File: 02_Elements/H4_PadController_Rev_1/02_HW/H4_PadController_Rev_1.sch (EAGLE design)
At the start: 42 parts

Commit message: Finished H4_PadController_Rev_1 Schematic
The Schematic has been finished! Yay!
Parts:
- added C_MUX: 10uF, adafruit:C-USC1206
- added J_PAD: 22-27-2101-10, con-molex:22-27-2101-10
- added J_PRG: 22-27-2051-05, con-molex:22-27-2051-05
- added R_BRIDGE: 220Ohm, adafruit:R-US_M1206
- added R_PAD_0, R_PAD_1: 0Ohm, adafruit:R-US_M1206
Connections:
- removed net GPIO16: J_AUX.5, X2.GPIO16
- removed net N$1: U_MUXA.X0
- removed net N$12: U_MUXA.X2
- removed net N$13: U_MUXA.X3
- removed net N$21: U_MUXA.X4
- removed net N$22: U_MUXA.X5
- removed net N$23: U_MUXA.X6
- removed net N$24: U_MUXA.X7
- removed net N$25: U_MUXA.INH
- removed net N$26: U_MUXA.A
- removed net N$27: U_MUXA.B
- removed net N$28: U_MUXA.C
- removed net N$29: U_MUXA.X
- removed net N$4: X2.TXD
- removed net N$6: U_MUXA.X1
- removed net N$7: X2.RXD
- new net MUX_A: J_AUX.5, U_MUXA.A, X2.GPIO16
- new net MUX_B: U_MUXA.B, X2.GPIO12
- new net MUX_C: U_MUXA.C, X2.GPIO13
- new net PAD_0: J_PAD-8.S, U_MUXA.X0
- new net PAD_1: J_PAD-7.S, U_MUXA.X1
- new net PAD_2: J_PAD-6.S, U_MUXA.X2
- new net PAD_3: J_PAD-5.S, U_MUXA.X3
- new net PAD_4: J_PAD-4.S, U_MUXA.X4
- new net PAD_5: J_PAD-3.S, U_MUXA.X5
- new net PAD_6: J_PAD-2.S, U_MUXA.X6
- new net PAD_7: J_PAD-1.S, U_MUXA.X7
- new net PAD_MUX: R_PAD_0.1, U_MUXA.X
- new net PAD_SINGLE: J_PAD-9.S, R_PAD_1.1
- new net RX: J_PRG-4.S, X2.RXD
- new net TX: J_PRG-3.S, X2.TXD
- net 3V3: now also C_MUX.1, J_PRG-5.S, R_BRIDGE.1, U_MUXA.INH, U_MUXP.VCC, U_MUXP.VEE
- net 5V: now also J_PRG-1.S
- net GND: now also C_MUX.2, J_PAD-10.S, J_PRG-2.S, U_MUXP.GND
- net GPIO12: no longer X2.GPIO12
- net GPIO13: no longer X2.GPIO13
- net PAD: now also R_BRIDGE.2, R_PAD_0.2, R_PAD_1.2
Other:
- note added: "CONNECTOR FOR EXTENDED BOARD"
- note added: "CONNECTOR FOR EXTENDED LEDS"
- note added: "CONNECTOR FOR INPUT SIGNALS AND POWER"
- note added: "CONNECTOR FOR PROGRAMMER"
- note added: "HENAR#4 PROJECT AUTOFABRICANTES www.autofabricantes.org"
- note added: "LED STRIPE"
- note added: "MULTIPLEXER AND RESISTOR BRIDGE"
- note added: "R_PAD_0 and R_PAD_1 are to select the Input PAD Analog Signal. In a normal situation, with only one Input, R_PAD_1 should be mounted."
- note removed: "DC MOTOR + POT"
- note removed: "DC Motor Drivers"
- note removed: "MYO-HAND PROJECT AUTOFABRICANTES www.autofabricantes.org"
- note removed: "WS2812B RGB LEDs"
- moved on the sheet: C_DC_0, C_DC_1, J_AUX, J_IN-1, J_IN-2, J_IN-3, J_IN-4, R_ESP5, R_ESP6, R_I2C_0, R_I2C_1, R_SET_0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

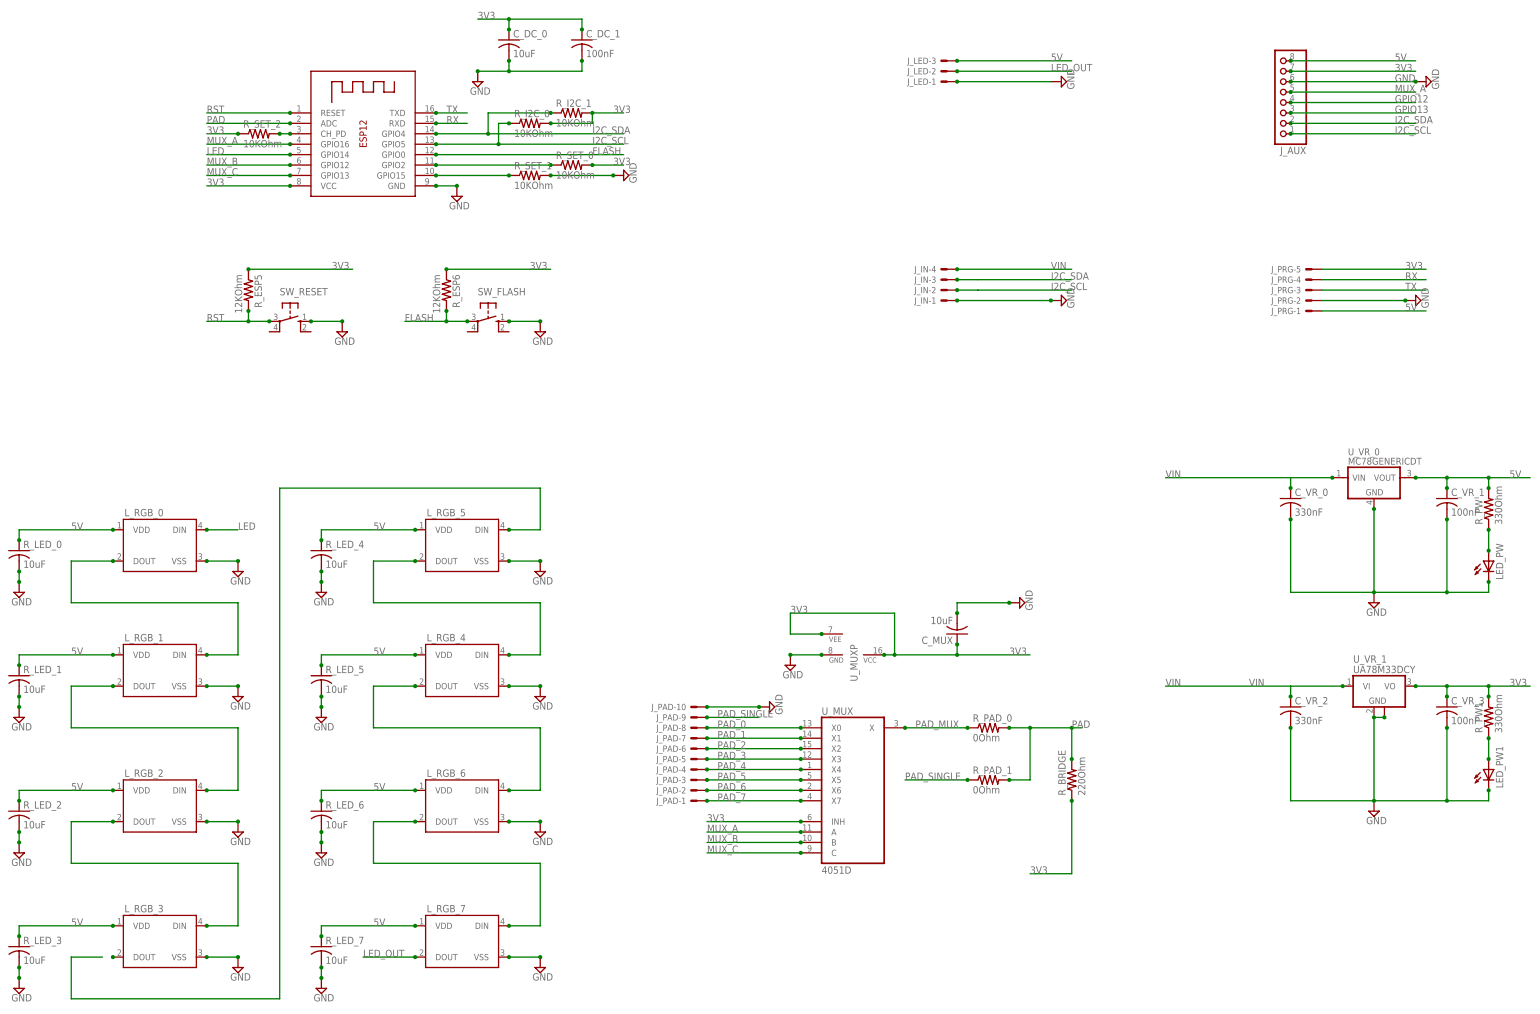
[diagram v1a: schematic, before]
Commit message: Finished Routing H4_PadController_Rev_1
Finished the Routing of the full Element H4_PadController_Rev_4.

Need to make Silk, 3D model, Gerber Files and BOM.
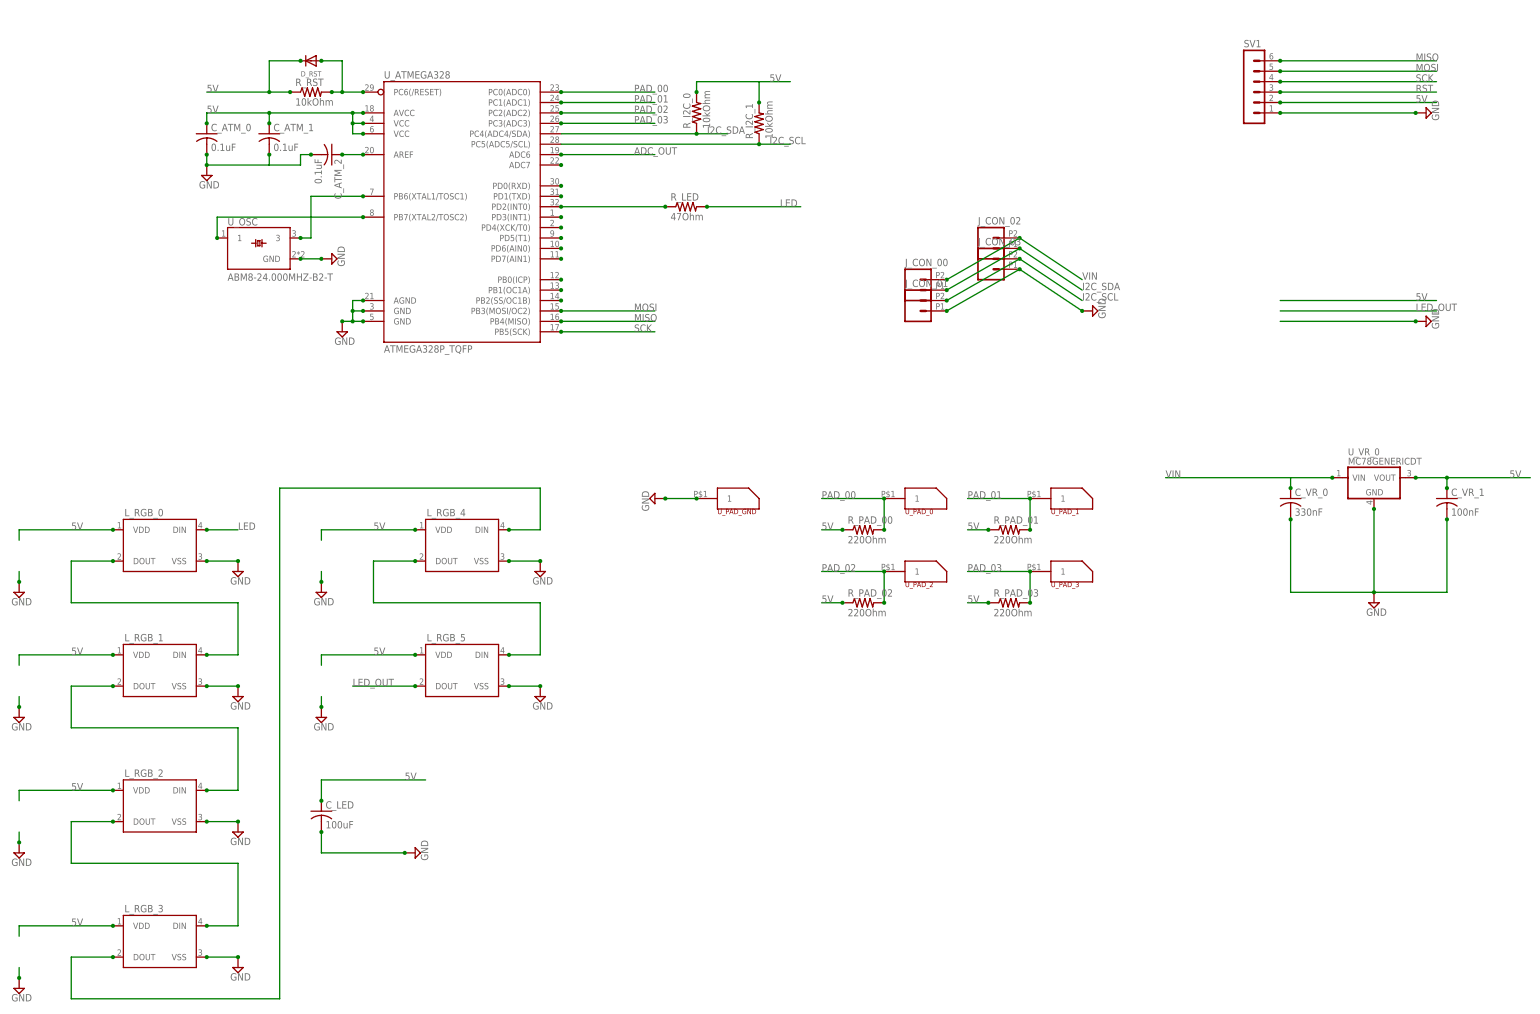
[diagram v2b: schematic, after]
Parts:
- removed C_DC_0, C_MUX, R_LED_0, R_LED_1, R_LED_2, R_LED_3, R_LED_4, R_LED_5, R_LED_6, R_LED_7: 10uF, adafruit:C-USC1206
- removed C_DC_1, C_VR_3: 100nF, adafruit:C-USC1206
- removed C_VR_2: 330nF, adafruit:C-USC1206
- removed J_AUX: (no value), adafruit:PINHD-1X8BIG
- removed J_IN: 22-05-7048-04, con-molex:22-05-7048-04
- removed J_LED: 22-05-7038-03, con-molex:22-05-7038-03
- removed J_PAD: 22-27-2101-10, con-molex:22-27-2101-10
- removed J_PRG: 22-27-2051-05, con-molex:22-27-2051-05
- removed LED_PW, LED_PW1: (no value), adafruit:LEDSMT1206
- removed L_RGB_6, L_RGB_7: (no value), SparkFun-LED:WS2812B
- removed R_BRIDGE: 220Ohm, adafruit:R-US_M1206
- removed R_ESP5, R_ESP6: 12KOhm, adafruit:R-US_M1206
- removed R_PAD_0, R_PAD_1: 0Ohm, adafruit:R-US_M1206
- removed R_PW, R_PW1: 330Ohm, adafruit:R-US_M1206
- removed R_SET_0, R_SET_1, R_SET_2: 10KOhm, adafruit:R-US_M1206
- removed SW_FLASH, SW_RESET: (no value), switch-omron:10-XX
- removed U_MUX: 4051D, 40xx:4051D
- removed U_VR_1: UA78M33DCY, linear:UA78M33DCY
- removed X2: (no value), adafruit:ESP-12
- added C_ATM_0, C_ATM_1, C_ATM_2: 0.1uF, adafruit:C-USC0805
- added C_LED: 100uF, adafruit:C-USC1210
- added D_RST: (no value), microbuilder:DIODESOD-123
- added J_CON_00, J_CON_01, J_CON_02, J_CON_03: (no value), SparkFun-Connectors:M022.54MM_SCREWTERM
- added R_LED: 47Ohm, adafruit:R-US_M0805
- added R_PAD_00, R_PAD_01, R_PAD_02, R_PAD_03: 220Ohm, adafruit:R-US_M0805
- added R_RST: 10kOhm, adafruit:R-US_M0805
- added SV1: (no value), con-lstb:MA06-1
- added U_ATMEGA328: ATMEGA328P_TQFP, SparkFun-DigitalIC:ATMEGA328P_TQFP
- added U_OSC: ABM8-24.000MHZ-B2-T, ABM8-24.000MHZ-B2-T:ABM8-24.000MHZ-B2-T
- added U_PAD_0, U_PAD_1, U_PAD_2, U_PAD_3, U_PAD_GND: PAD_CONNECTOR_MULTI, atfHenar_customLib:PAD_CONNECTOR_MULTI
- C_VR_0, C_VR_1: device adafruit:C-USC1206 -> adafruit:C-USC0805
- R_I2C_0, R_I2C_1: value 10KOhm -> 10kOhm; device adafruit:R-US_M1206 -> adafruit:R-US_M0805
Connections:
- removed net 3V3: C_DC_0.1, C_DC_1.1, C_MUX.1, C_VR_3.1, J_AUX.7, J_PRG-5.S, R_BRIDGE.1, R_ESP5.1, R_ESP6.1, R_I2C_0.2, R_I2C_1.2, R_PW1.2, R_SET_0.2, R_SET_2.1, U_MUXA.INH, U_MUXP.VCC, U_MUXP.VEE, U_VR_1.VO, X2.VCC
- removed net FLASH: R_ESP6.2, SW_FLASH.P, X2.GPIO0
- removed net GPIO12: J_AUX.4
- removed net GPIO13: J_AUX.3
- removed net MUX_A: J_AUX.5, U_MUXA.A, X2.GPIO16
- removed net MUX_B: U_MUXA.B, X2.GPIO12
- removed net MUX_C: U_MUXA.C, X2.GPIO13
- removed net N$11: L_RGB_3.DOUT
- removed net N$15: J_IN-2.S
- removed net PAD: R_BRIDGE.2, R_PAD_0.2, R_PAD_1.2, X2.ADC
- removed net PAD_0: J_PAD-8.S, U_MUXA.X0
- removed net PAD_1: J_PAD-7.S, U_MUXA.X1
- removed net PAD_2: J_PAD-6.S, U_MUXA.X2
- removed net PAD_3: J_PAD-5.S, U_MUXA.X3
- removed net PAD_4: J_PAD-4.S, U_MUXA.X4
- removed net PAD_5: J_PAD-3.S, U_MUXA.X5
- removed net PAD_6: J_PAD-2.S, U_MUXA.X6
- removed net PAD_7: J_PAD-1.S, U_MUXA.X7
- removed net PAD_MUX: R_PAD_0.1, U_MUXA.X
- removed net PAD_SINGLE: J_PAD-9.S, R_PAD_1.1
- removed net RX: J_PRG-4.S, X2.RXD
- removed net TX: J_PRG-3.S, X2.TXD
- new net ADC_OUT: U_ATMEGA328.ADC6
- new net LEDE: L_RGB_3.DOUT, L_RGB_4.DIN
- new net MISO: SV1.6, U_ATMEGA328.PB4(MISO)
- new net MOSI: SV1.5, U_ATMEGA328.PB3(MOSI/OC2)
- new net N$1: U_ATMEGA328.PD0(RXD)
- new net N$13: U_ATMEGA328.ADC7
- new net N$21: U_ATMEGA328.PB0(ICP)
- new net N$22: U_ATMEGA328.PB1(OC1A)
- new net N$23: U_ATMEGA328.PB2(SS/OC1B)
- new net N$4: C_ATM_2.1, U_ATMEGA328.AREF
- new net N$6: U_ATMEGA328.PD1(TXD)
- new net PAD_00: R_PAD_00.2, U_ATMEGA328.PC0(ADC0), U_PAD_0.1
- new net PAD_01: R_PAD_01.2, U_ATMEGA328.PC1(ADC1), U_PAD_1.1
- new net PAD_02: R_PAD_02.2, U_ATMEGA328.PC2(ADC2), U_PAD_2.1
- new net PAD_03: R_PAD_03.2, U_ATMEGA328.PC3(ADC3), U_PAD_3.1
- new net SCK: SV1.4, U_ATMEGA328.PB5(SCK)
- net 5V: now also C_ATM_0.1, C_ATM_1.1, C_LED.1, D_RST.C, R_I2C_0.2, R_I2C_1.2, R_PAD_00.1, R_PAD_01.1, R_PAD_02.1, R_PAD_03.1, R_RST.1, SV1.2, U_ATMEGA328.AVCC, U_ATMEGA328.VCC@4, U_ATMEGA328.VCC@6; no longer J_AUX.8, J_LED-3.S, J_PRG-1.S, L_RGB_6.VDD, L_RGB_7.VDD, R_LED_0.1, R_LED_1.1, R_LED_2.1, R_LED_3.1, R_LED_4.1, R_LED_5.1, R_LED_6.1, R_LED_7.1, R_PW.2
- net GND: now also C_ATM_0.2, C_ATM_1.2, C_ATM_2.2, C_LED.2, J_CON_01.1, J_CON_03.1, SV1.1, U_ATMEGA328.AGND, U_ATMEGA328.GND@3, U_ATMEGA328.GND@5, U_OSC.GND, U_PAD_GND.1; no longer C_DC_0.2, C_DC_1.2, C_MUX.2, C_VR_2.2, C_VR_3.2, J_AUX.6, J_IN-1.S, J_LED-1.S, J_PAD-10.S, J_PRG-2.S, LED_PW.C, LED_PW1.C, L_RGB_6.VSS, L_RGB_7.VSS, R_LED_0.2, R_LED_1.2, R_LED_2.2, R_LED_3.2, R_LED_4.2, R_LED_5.2, R_LED_6.2, R_LED_7.2, R_SET_1.2, SW_FLASH.S, SW_RESET.S, U_MUXP.GND, U_VR_1.GND, U_VR_1.GND@1, X2.GND
- net I2C_SCL: now also J_CON_01.2, J_CON_03.2, R_I2C_1.1, U_ATMEGA328.PC5(ADC5/SCL); no longer J_AUX.1, R_I2C_0.1, X2.GPIO5
- net I2C_SDA: now also J_CON_00.1, J_CON_02.1, R_I2C_0.1, U_ATMEGA328.PC4(ADC4/SDA); no longer J_AUX.2, R_I2C_1.1, X2.GPIO4
- net LED: now also R_LED.2; no longer L_RGB_5.DIN, X2.GPIO14
- net LED_OUT: now also L_RGB_5.DOUT; no longer J_LED-2.S, L_RGB_7.DOUT
- net N$14: now also L_RGB_4.DOUT, L_RGB_5.DIN; no longer L_RGB_4.DIN, L_RGB_5.DOUT
- net N$16: now also U_ATMEGA328.PD3(INT1); no longer J_IN-3.S
- net N$17: now also U_ATMEGA328.PD4(XCK/T0); no longer L_RGB_4.DOUT, L_RGB_6.DIN
- net N$18: now also U_ATMEGA328.PD5(T1); no longer R_SET_0.1, X2.GPIO2
- net N$19: now also U_ATMEGA328.PD6(AIN0); no longer R_SET_1.1, X2.GPIO15
- net N$2: now also U_ATMEGA328.PB6(XTAL1/TOSC1), U_OSC.3; no longer R_SET_2.2, X2.CH_PD
- net N$20: now also U_ATMEGA328.PD7(AIN1); no longer L_RGB_6.DOUT, L_RGB_7.DIN
- net N$5: now also U_ATMEGA328.PB7(XTAL2/TOSC2), U_OSC.1; no longer LED_PW.A, R_PW.1
- net N$8: now also R_LED.1, U_ATMEGA328.PD2(INT0); no longer LED_PW1.A, R_PW1.1
- net RST: now also D_RST.A, R_RST.2, SV1.3, U_ATMEGA328.PC6(/RESET); no longer R_ESP5.2, SW_RESET.P, X2.RESET
- net VIN: now also J_CON_00.2, J_CON_02.2; no longer C_VR_2.1, J_IN-4.S, U_VR_1.VI
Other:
- note added: "ATMEGA328"
- note added: "This Schematic is heavily based on: http://www.gammon.com.au/images/Wire_Wrapped_Atmega132_e.png"
- note removed: "CONNECTOR FOR EXTENDED LEDS"
- note removed: "ESP12"
- note removed: "Power Input 3V3"
- note removed: "This Schematic is heavily based on: https://dl.espressif.com/dl/schematics/ESP32-Core-Board-V2_sch.pdf"
- moved on the sheet: L_RGB_4, L_RGB_5, R_I2C_0, R_I2C_1

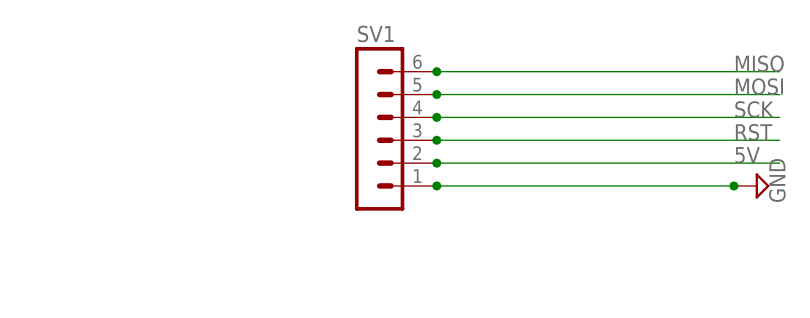
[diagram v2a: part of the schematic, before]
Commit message: H4_PadController_Rev_1 Finished Layout, Gerber Files and 3D Model
The PCB has been finished and the Layout, Gerber Files and 3D Model Finished.

TODO:
Make a better Schematic
Make a good BOM
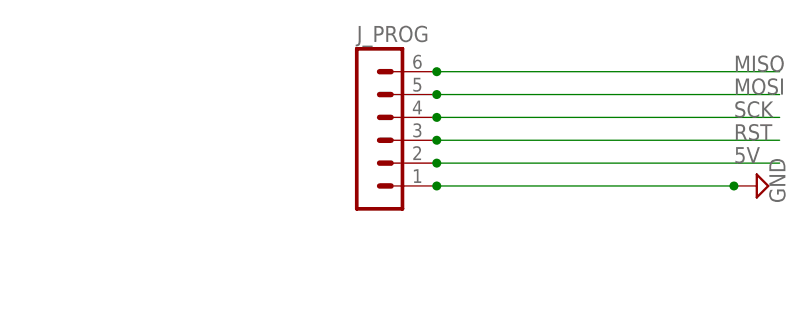
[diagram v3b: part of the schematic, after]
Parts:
- renumbered SV1 to J_PROG
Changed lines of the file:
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@@
 <part name="C_LED" library="adafruit" deviceset="C-US" device="C1210" value="100uF"/>
 <part name="R_LED" library="adafruit" deviceset="R-US_" device="M0805" value="47Ohm"/>
-<part name="SV1" library="con-lstb" deviceset="MA06-1" device=""/>
+<part name="J_PROG" library="con-lstb" deviceset="MA06-1" device=""/>
 <part name="SUPPLY7" library="supply2" deviceset="GND" device=""/>
 <part name="SUPPLY8" library="supply2" deviceset="GND" device=""/>
@@
 <instance part="C_LED" gate="G$1" x="86.36" y="55.88"/>
 <instance part="R_LED" gate="G$1" x="175.26" y="203.2"/>
-<instance part="SV1" gate="1" x="312.42" y="233.68"/>
+<instance part="J_PROG" gate="1" x="312.42" y="233.68"/>
 <instance part="SUPPLY7" gate="GND" x="355.6" y="226.06" rot="R90"/>
 <instance part="SUPPLY8" gate="GND" x="355.6" y="175.26" rot="R90"/>
@@
 </segment>
 <segment>
-<pinref part="SV1" gate="1" pin="1"/>
+<pinref part="J_PROG" gate="1" pin="1"/>
 <pinref part="SUPPLY7" gate="GND" pin="GND"/>
 <wire x1="320.04" y1="226.06" x2="353.06" y2="226.06" width="0.1524" layer="91"/>
@@
 </segment>
 <segment>
-<pinref part="SV1" gate="1" pin="2"/>
+<pinref part="J_PROG" gate="1" pin="2"/>
 <wire x1="358.14" y1="228.6" x2="320.04" y2="228.6" width="0.1524" layer="91"/>
 <label x="353.06" y="228.6" size="1.778" layer="95"/>
@@
 </segment>
 <segment>
-<pinref part="SV1" gate="1" pin="5"/>
+<pinref part="J_PROG" gate="1" pin="5"/>
 <wire x1="358.14" y1="236.22" x2="320.04" y2="236.22" width="0.1524" layer="91"/>
 <label x="353.06" y="236.22" size="1.778" layer="95"/>
@@
 </segment>
 <segment>
-<pinref part="SV1" gate="1" pin="6"/>
+<pinref part="J_PROG" gate="1" pin="6"/>
 <wire x1="358.14" y1="238.76" x2="320.04" y2="238.76" width="0.1524" layer="91"/>
 <label x="353.06" y="238.76" size="1.778" layer="95"/>
@@
 </segment>
 <segment>
-<pinref part="SV1" gate="1" pin="4"/>
+<pinref part="J_PROG" gate="1" pin="4"/>
 <wire x1="358.14" y1="233.68" x2="320.04" y2="233.68" width="0.1524" layer="91"/>
 <label x="353.06" y="233.68" size="1.778" layer="95"/>
@@
 <net name="RST" class="0">
 <segment>
-<pinref part="SV1" gate="1" pin="3"/>
+<pinref part="J_PROG" gate="1" pin="3"/>
 <wire x1="358.14" y1="231.14" x2="320.04" y2="231.14" width="0.1524" layer="91"/>
 <label x="353.06" y="231.14" size="1.778" layer="95"/>
